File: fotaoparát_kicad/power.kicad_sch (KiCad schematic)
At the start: 57 parts

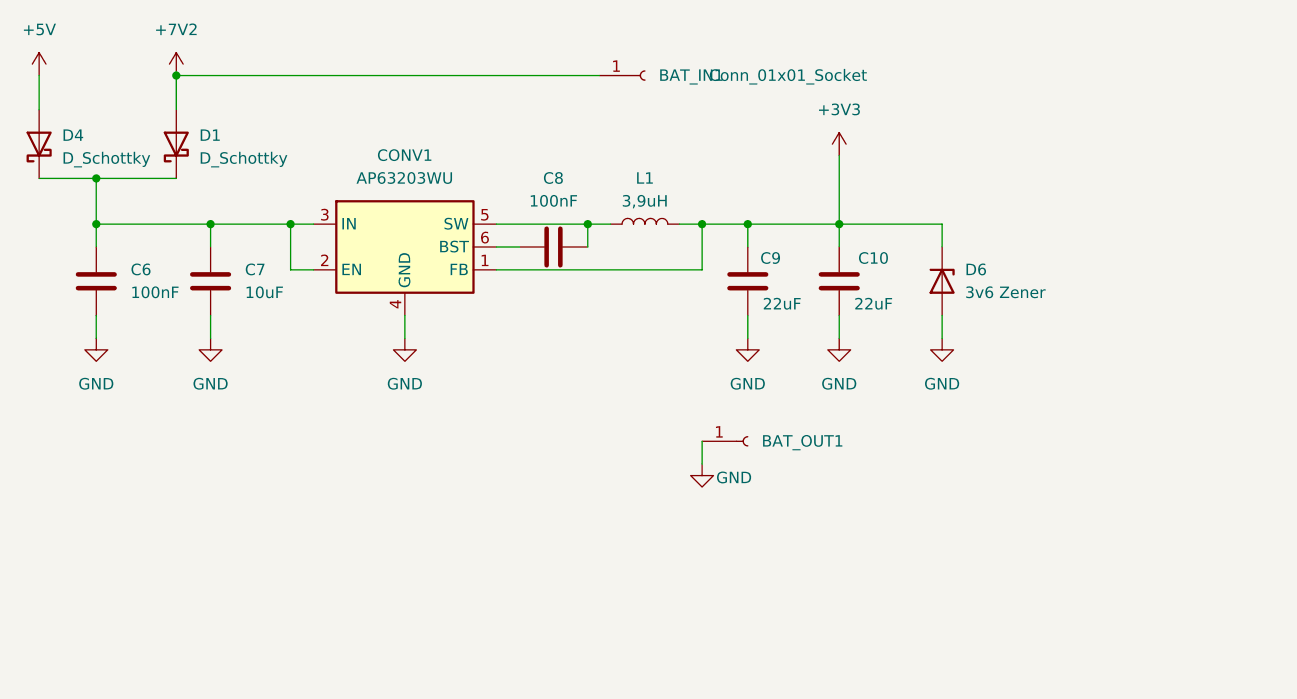
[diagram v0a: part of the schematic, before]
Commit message: Přidal jsem dokumentaci, asi se mi git vykálí do obličeje při mergi, ale neva.
Dostal jsem se k Flash paměti

Co-authored-by: Copilot <copilot@github.com>
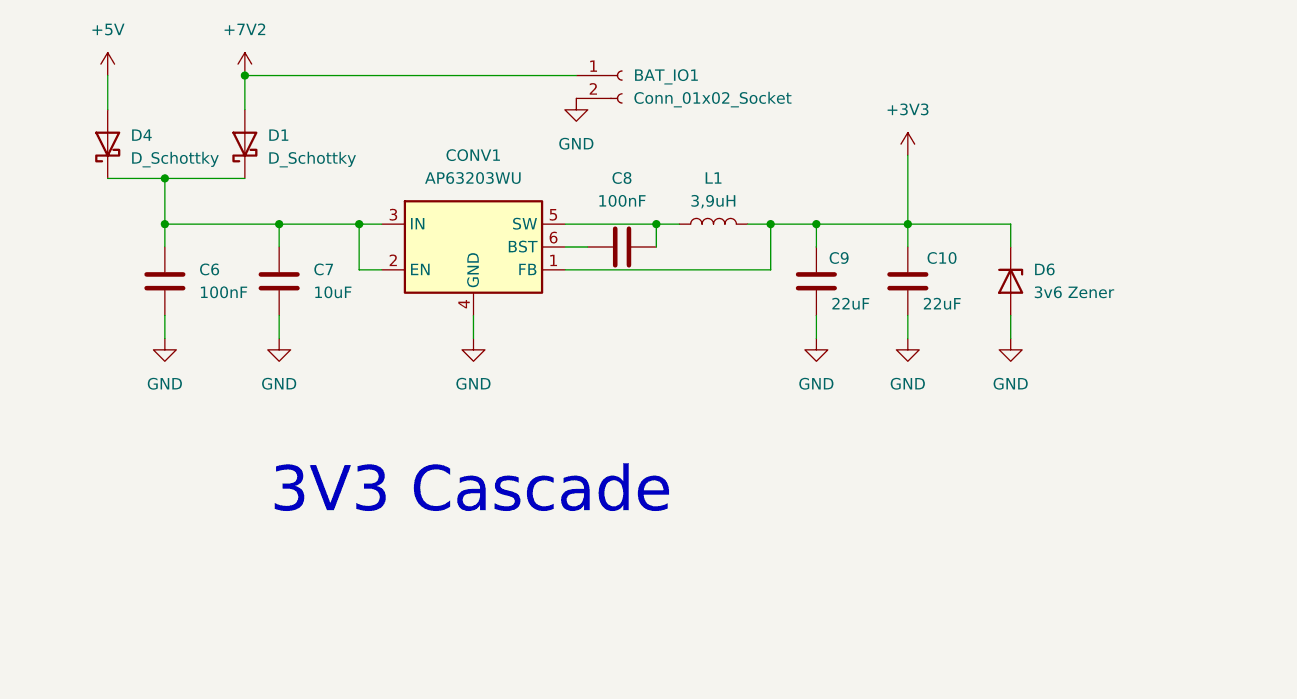
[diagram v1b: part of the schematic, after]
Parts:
- removed BAT_IN1, BAT_OUT1: Conn_01x01_Socket, Connector_Wire:SolderWirePad_1x01_SMD_1.5x3mm, symbol Connector:Conn_01x01_Socket
- added BAT_IO1: Conn_01x02_Socket, Connector_Wire:SolderWire-1.5sqmm_1x02_P6mm_D1.7mm_OD3mm, symbol Connector:Conn_01x02_Socket
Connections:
- net +7V2: now also BAT_IO1.1 (Pin_1)
- net GND: now also BAT_IO1.2 (Pin_2)
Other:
- note added: "3V3 Cascade"
- moved on the sheet: C10, C6, C7, C8, C9, CONV1, D1, D4, D6, L1
